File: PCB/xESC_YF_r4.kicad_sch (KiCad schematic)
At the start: 50 parts, among them J1 Conn_01x09_Male, J10 OM-MB W => MC BRK, J2 Conn_01x03_Pin, J3 Conn_01x05_Male, J4 Conn_01x05_Male, J6 OM-MB U <= MC SA, J7 Conn_01x06_Male, J8 Conn_01x06_Pin, J9 OM-MB V => MC +24V, Q1 2N7002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

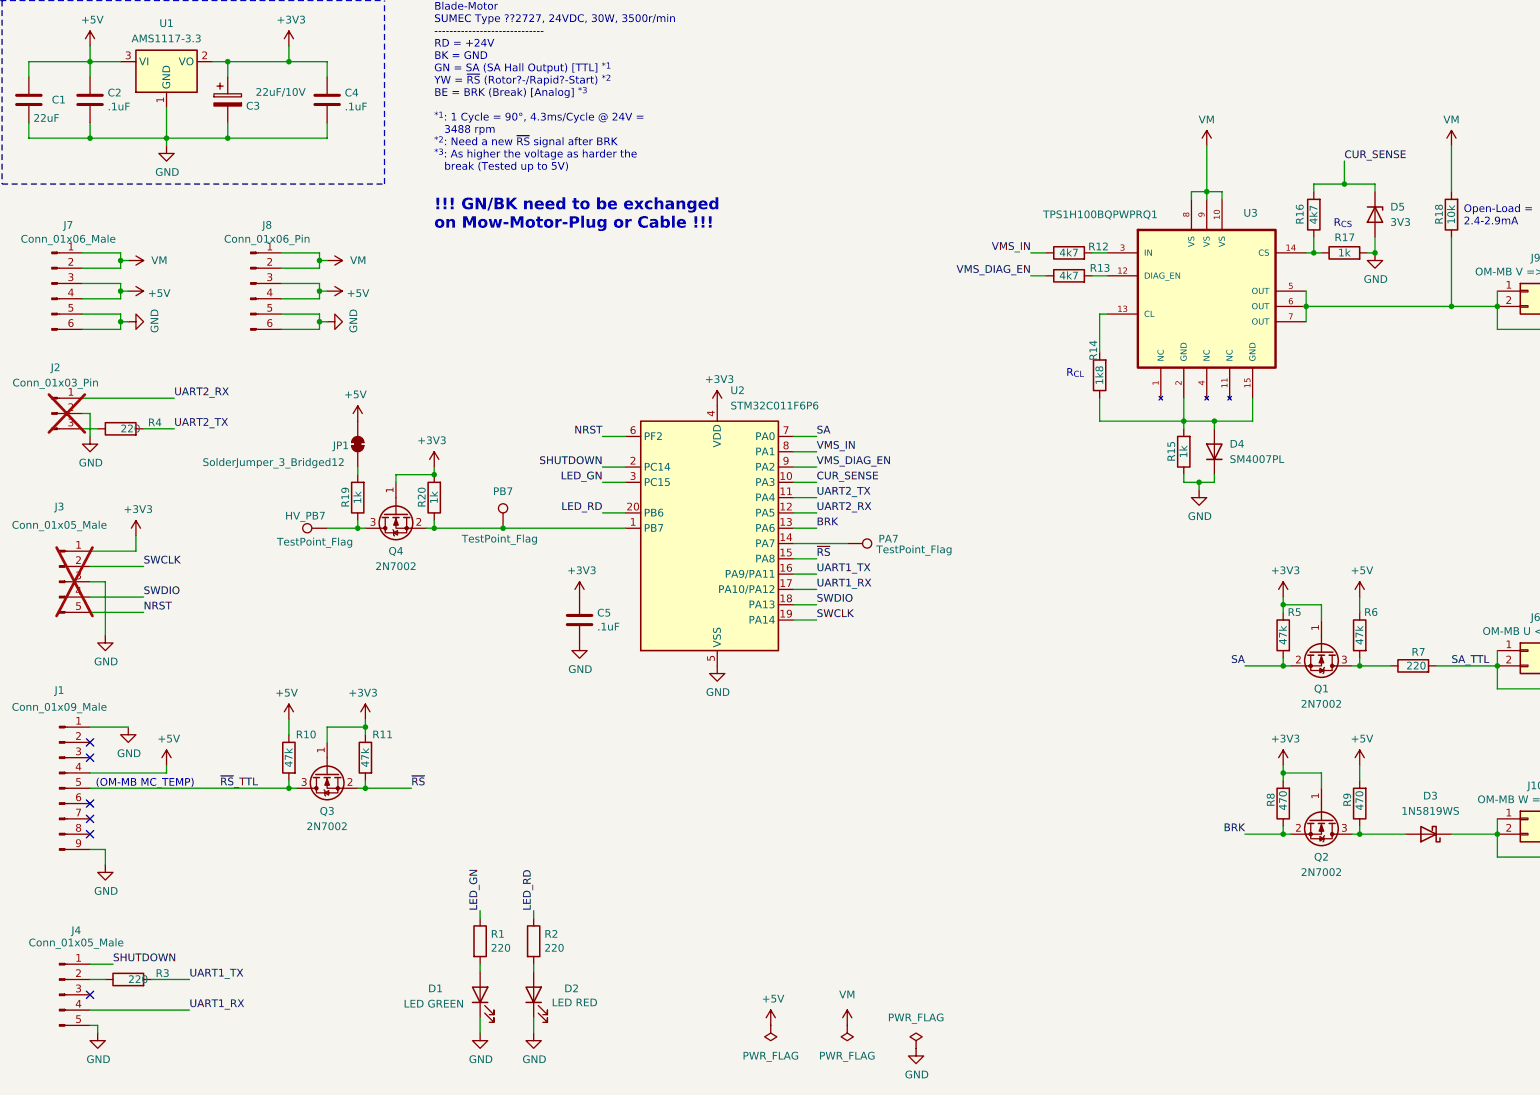
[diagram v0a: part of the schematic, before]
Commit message: ✨ feat(xESC_YF_r4): add hardware version 2 support
- add conditional compilation in firmware for hardware versions 1 and 2
- update GPIO mappings and ADC channel assignments for version 2 hardware
- add new hardware version 2 image to documentation
- update README with hardware version 2 information and installation instructions
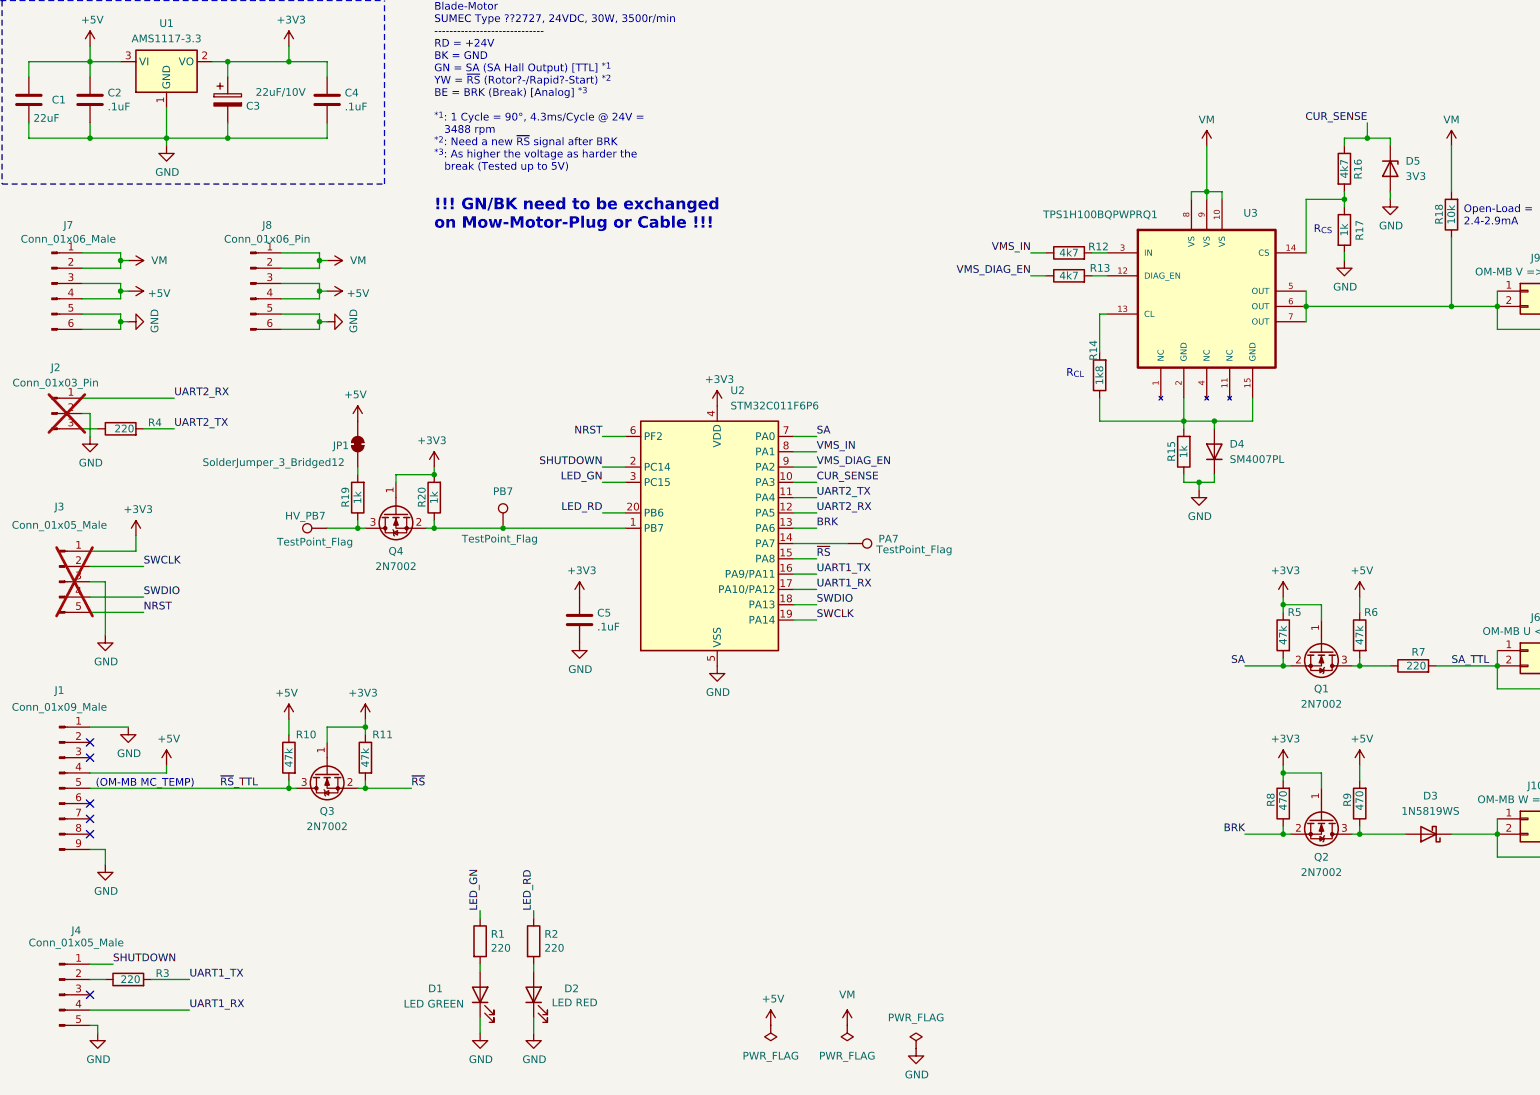
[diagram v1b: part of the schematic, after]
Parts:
- R1, R2, R3, R4, R7: value 220 -> 220
- R8, R9: value 470 -> 470
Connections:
- net CUR_SENSE: now also R16.1; no longer R16.2
- net at R17.1, U3.14 (CS): now also R16.2; no longer R16.1
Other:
- moved on the sheet: D5, R16, R17

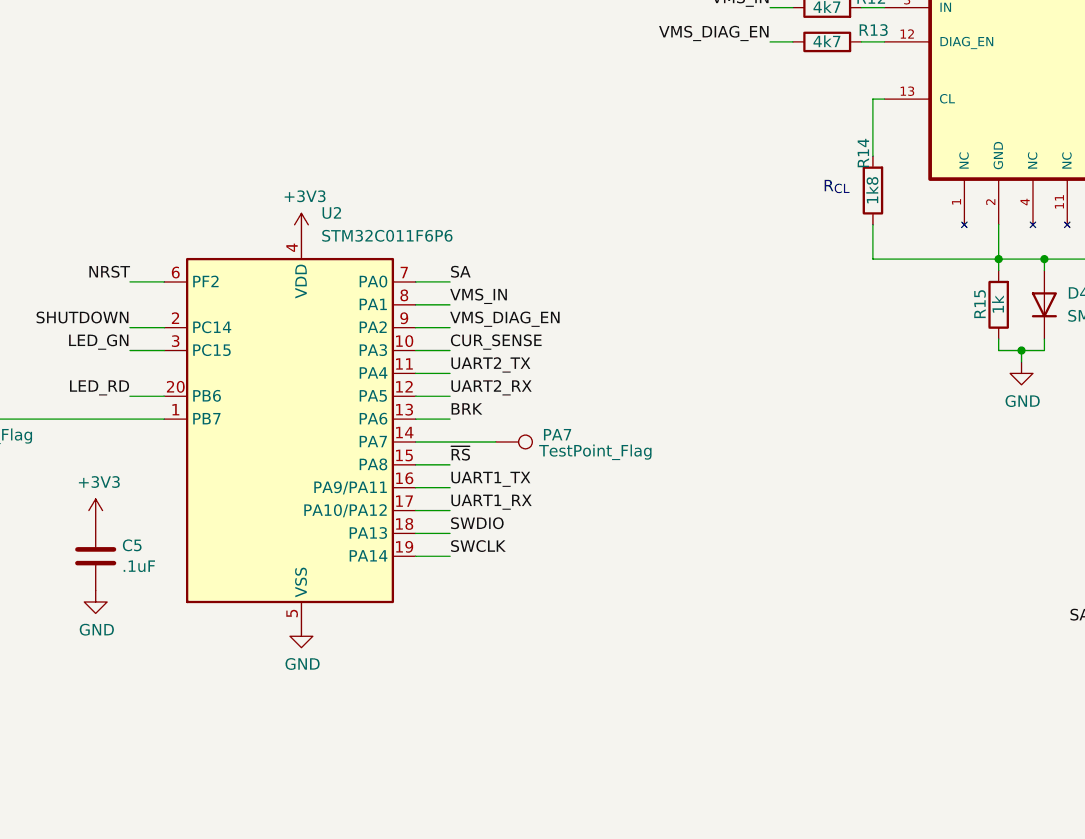
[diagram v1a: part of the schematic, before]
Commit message: Fix ERC/DRC
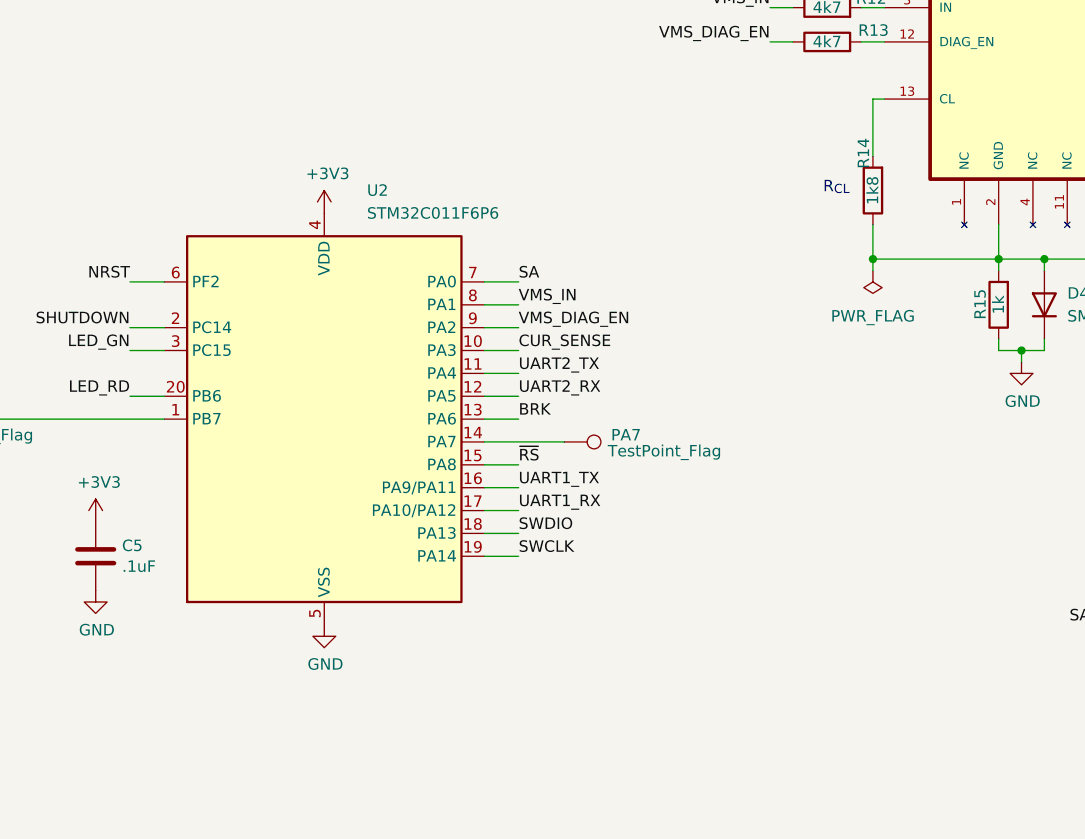
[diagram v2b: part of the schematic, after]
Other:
- moved on the sheet: PA7, U2
